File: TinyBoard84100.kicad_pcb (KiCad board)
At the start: 2 copper layers, 25.7 x 15.2 mm, 13 parts, among them P2 CONN_01X07, P3 CONN_01X07, P4 CONN_02X03, SW1 SW_PUSH, U1 78L05, U2 ATTINY841

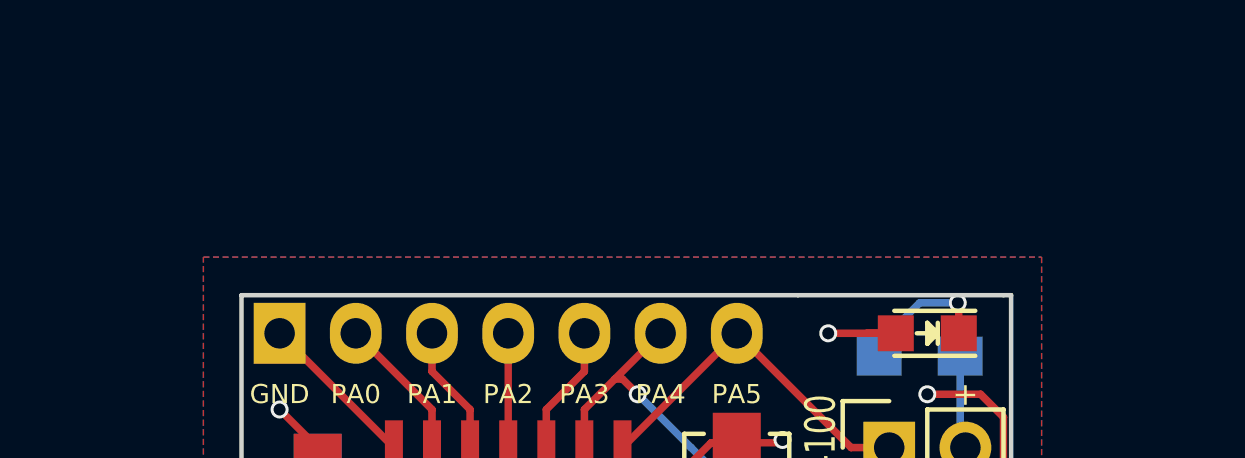
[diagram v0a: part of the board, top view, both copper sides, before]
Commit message: update warning
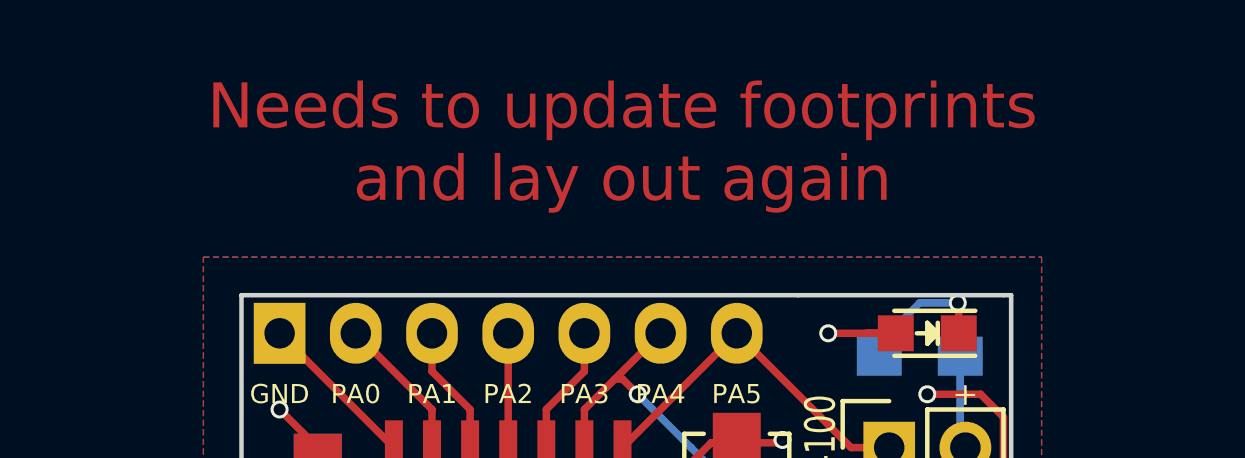
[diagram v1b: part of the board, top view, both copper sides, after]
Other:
- board text added: "Needs to update footprints and lay out again"
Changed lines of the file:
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@@
     (area 151.171 68.875 185.453143 91.393333)
     (thickness 1.6)
-    (drawings 29)
+    (drawings 30)
     (tracks 116)
     (zones 0)
@@
     )
   )
+  (gr_text "Needs to update footprints\nand lay out again" (at 168.91 67.31) (layer F.Cu)
+    (effects (font (size 1.5 1.5) (thickness 0.3)))
+  )
   (gr_text 04/18 (at 156.845 80.01 90) (layer B.SilkS)

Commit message: starting over
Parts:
- C1, P2, P3, R1, R2, R3: moved to F.Cu
- SW1: footprint Buttons_Switches_SMD:SW_SPST_EVQPE1 -> Buttons_Switches_SMD:SW_SPST_FSMSM
- U1: footprint TO_SOT_Packages_SMD:SOT-23_Handsoldering -> TO_SOT_Packages_SMD:SOT89-3_Housing_Handsoldering; moved to F.Cu
- moved C2 39.1 mm to (192.2, 100.2), turned to 0 degrees
- moved C1 36.1 mm to (192.2, 93.5), turned to 0 degrees
- moved U1 32.1 mm to (197.1, 83.4), turned to 0 degrees
- moved R2 27.5 mm to (184.2, 101.3), turned to 0 degrees
- moved U2 25.6 mm to (190.4, 83.8), turned to 0 degrees
- moved D1 23.6 mm to (201.7, 80.2), turned to 0 degrees
- moved D2 22.6 mm to (201.7, 85.7)
- moved R1 22.6 mm to (179.0, 101.3)
- moved R3 22.5 mm to (198.4, 92.9)
- moved SW1 17.2 mm to (182.5, 94.2), turned to 0 degrees
- moved P3 17.0 mm to (171.3, 83.5), turned to 0 degrees
- moved P4 7.04 mm to (181.4, 83.5)
- moved P2 4.70 mm to (161.2, 83.5), turned to 0 degrees
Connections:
- C1 pad 1: Net-(C1-Pad1) -> +BATT
- C2 pad 1: Net-(C1-Pad1) -> +BATT
- P2 pad 1: +5V -> +BATT
- U1 pad 3: Net-(C1-Pad1) -> +BATT
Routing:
- net GND: track 25.8 -> 0.00 mm, vias 6 -> 0
- net /PA4: track 22.6 -> 0.00 mm, vias 1 -> 0
- net /PB3: track 22.5 -> 0.00 mm, vias 2 -> 0
- net +5V: track 17.7 -> 0.00 mm, vias 2 -> 0
- net /PA6: track 16.9 -> 0.00 mm, vias 1 -> 0
- net /PA5: track 12.0 -> 0.00 mm
- net Net-(C1-Pad1): track 5.68 -> 0.00 mm, vias 1 -> 0
- net /PA7: track 4.70 -> 0.00 mm
- net /PB0: track 4.70 -> 0.00 mm
- net /PA0: track 4.70 -> 0.00 mm
- net Net-(D1-Pad1): track 4.64 -> 0.00 mm, vias 1 -> 0
- net /PA1: track 4.18 -> 0.00 mm
- net /PB1: track 4.18 -> 0.00 mm
- net /PA3: track 4.18 -> 0.00 mm
- net /PB2: track 4.18 -> 0.00 mm
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- removed copper zone on F.Cu, net +5V
- removed copper zone on B.Cu, net GND
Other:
- board outline removed
- board text added: "All to be done from scratch"
- board text removed: "+"
- board text removed: "-"
- board text removed: "04/18"
- board text removed: "5V"
- board text removed: "GND"
- board text removed: "Needs to update footprints and lay out again"
- board text removed: "PA0"
- board text removed: "PA1"
- board text removed: "PA2"
- board text removed: "PA3"
- board text removed: "PA4"
- board text removed: "PA5"
- board text removed: "PA6"
- board text removed: "PA7"
- board text removed: "PB0"
- board text removed: "PB1"
- board text removed: "PB2"
- board text removed: "PB3"
- board text removed: "Rev2"
- board text removed: "TinyBoard84100"
- board text removed: "Unregulated Powersupply"

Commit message: first ideas
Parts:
- C2, R1, R2, R3, U1: moved to B.Cu
- moved U1 31.2 mm to (177.8, 108.0), turned to 270 degrees
- moved C2 29.3 mm to (163.8, 92.7), turned to 90 degrees
- moved C1 22.0 mm to (170.2, 92.7), turned to 90 degrees
- moved R3 20.4 mm to (190.5, 111.8)
- moved P2 18.6 mm to (171.4, 99.1), turned to 90 degrees
- moved U2 16.5 mm to (176.5, 92.7), turned to 90 degrees
- moved D2 13.5 mm to (195.6, 97.8), turned to 90 degrees
- moved R1 13.3 mm to (190.5, 108.0)
- moved D1 9.63 mm to (195.6, 87.6), turned to 90 degrees
- moved SW1 9.38 mm to (191.8, 92.7), turned to 270 degrees
- moved P4 7.19 mm to (184.2, 90.2)
- moved R2 6.89 mm to (190.5, 104.1)
- moved P3 2.82 mm to (171.4, 86.4), turned to 90 degrees
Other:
- board text added: "First idea"

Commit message: condensation
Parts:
- moved R1 15.3 mm to (191.8, 92.7)
- moved R3 15.3 mm to (191.8, 96.5)
- moved U1 15.3 mm to (176.5, 92.7)
- moved R2 15.3 mm to (191.8, 88.9)
- moved C2 6.35 mm to (170.2, 92.7)
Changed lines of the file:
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@@
   )
   (module Capacitors_SMD:C_1206_HandSoldering (layer B.Cu)
-    (at 163.83 92.71 90)
+    (at 170.18 92.71 90)
     (descr "Capacitor SMD 1206, hand soldering")
     (tags "capacitor 1206")
@@
   )
   (module Resistors_SMD:R_0805_HandSoldering (layer B.Cu)
-    (at 190.5 107.95)
+    (at 191.77 92.71)
     (descr "Resistor SMD 0805, hand soldering")
     (tags "resistor 0805")
@@
   )
   (module Resistors_SMD:R_0805_HandSoldering (layer B.Cu)
-    (at 190.5 104.14)
+    (at 191.77 88.9)
     (descr "Resistor SMD 0805, hand soldering")
     (tags "resistor 0805")
@@
   )
   (module Resistors_SMD:R_0805_HandSoldering (layer B.Cu)
-    (at 190.5 111.76)
+    (at 191.77 96.52)
     (descr "Resistor SMD 0805, hand soldering")
     (tags "resistor 0805")
@@
   )
   (module TO_SOT_Packages_SMD:SOT89-3_Housing_Handsoldering (layer B.Cu)
-    (at 177.8 107.95 270)
+    (at 176.53 92.71 270)
     (descr "SOT89-3, Housing, Handsoldering,")
     (tags "SOT89-3, Housing, Handsoldering,")

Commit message: almost finished layout
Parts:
- P2, P3: moved to B.Cu
- turned P2 to 270 degrees
- turned P3 to 270 degrees
- turned U1 to 90 degrees
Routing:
- net GND: track 0.00 -> 46.0 mm, vias 0 -> 4
- net /PB3: track 0.00 -> 28.1 mm, vias 0 -> 1
- net +5V: track 0.00 -> 26.0 mm, vias 0 -> 1
- net /PA4: track 0.00 -> 21.6 mm, vias 0 -> 1
- net /PA6: track 0.00 -> 18.1 mm, vias 0 -> 1
- net +BATT: track 0.00 -> 16.5 mm, vias 0 -> 1
- net /PA5: track 0.00 -> 8.74 mm
- net /PA7: track 0.00 -> 7.09 mm
- net /PA3: track 0.00 -> 5.97 mm
- net /PB2: track 0.00 -> 5.97 mm
- net /PA2: track 0.00 -> 4.85 mm
- net Net-(D1-Pad1): track 0.00 -> 4.52 mm, vias 0 -> 1
- net Net-(D2-Pad1): track 0.00 -> 4.36 mm, vias 0 -> 1
- net /PB1: track 0.00 -> 4.18 mm
- net /PA1: track 0.00 -> 4.18 mm
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- added copper zone on F.Cu, net +5V
- added copper zone on B.Cu, net GND
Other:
- board outline added: 27.9 x 15.2 mm
- board text added: "-"
- board text added: "PA0"
- board text added: "PA1"
- board text added: "PA2"
- board text added: "PA3"
- board text added: "PA4"
- board text added: "PA5"

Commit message: layout finished
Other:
- board text added: "+"
- board text added: "05/18"
- board text added: "5V"
- board text added: "GND"
- board text added: "ON"
- board text added: "PA6"
- board text added: "PA7"
- board text added: "PB0"
- board text added: "PB1"
- board text added: "PB2"
- board text added: "PB3"
- board text added: "Powersupply"
- board text added: "RST"
- board text added: "Rev3"
- board text added: "Tinyboard84100"
- board text added: "Unregulated"
- board text removed: "All to be done from scratch"
- board text removed: "First idea"
